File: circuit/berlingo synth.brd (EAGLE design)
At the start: 76.2 x 76.2 mm, 59 parts, among them IC4 LM358N, SW1 OS102011MA1Q

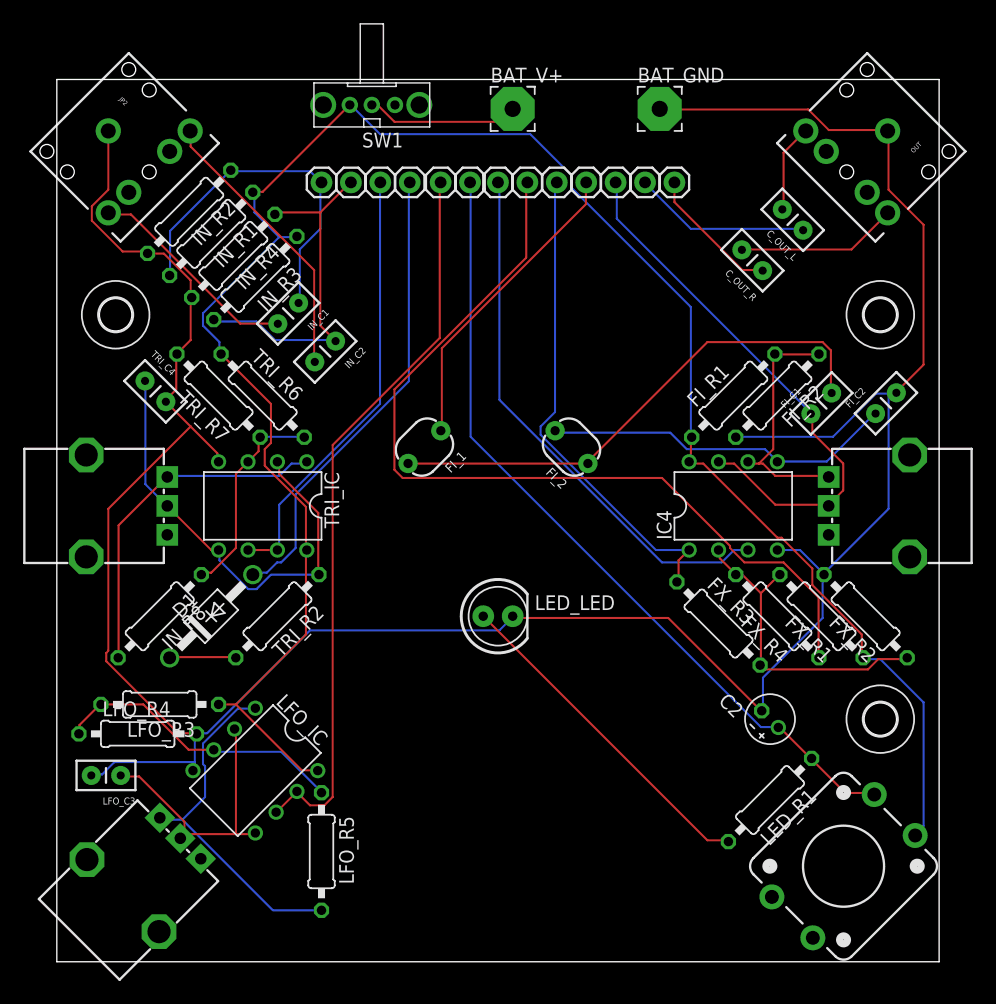
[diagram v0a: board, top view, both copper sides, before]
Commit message: Updated Parts and changed a few part names
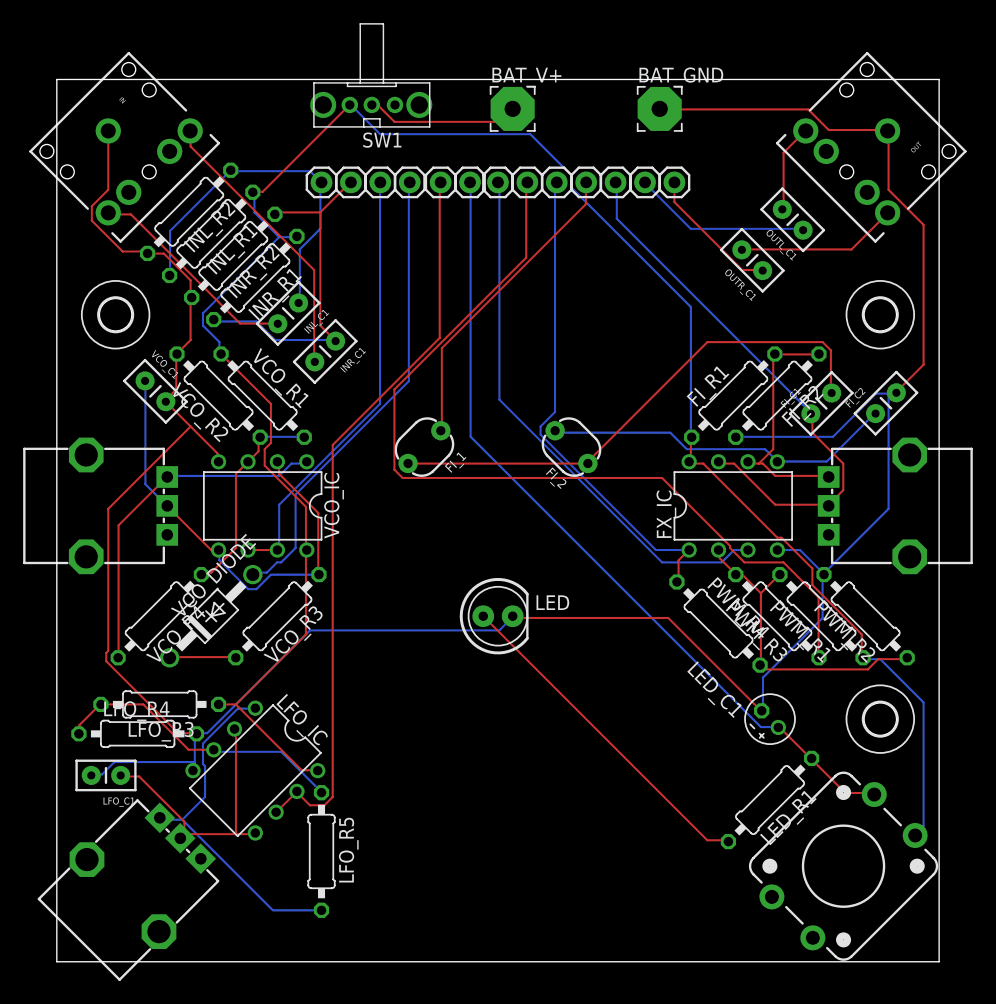
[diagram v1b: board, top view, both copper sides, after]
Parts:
- renumbered C2 to LED_C1, C_OUT_L to OUTL_C1, C_OUT_R to OUTR_C1, D1 to VCO_DIODE, FX_R1 to PWM_R1, FX_R2 to PWM_R2, FX_R3 to PWM_R4, FX_R4 to PWM_R3, IC4 to FX_IC, IN_C1 to INL_C1, IN_C2 to INR_C1, IN_L to INL, IN_R to INR, IN_R1 to INL_R1, IN_R2 to INL_R2, IN_R3 to INR_R1, IN_R4 to INR_R2, IN_R8 to VCO_R4, JP2 to IN, LED_LED to LED, LFO_C3 to LFO_C1, OUTA to OUTL, OUTB to OUTR, TRI_C4 to VCO_C1, TRI_IC to VCO_IC, TRI_PITCH to VCO_PITCH, TRI_R2 to VCO_R3, TRI_R6 to VCO_R1, TRI_R7 to VCO_R2, ~VCO to VCO~
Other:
- board text added: "Use eagle 6.6 to export!"
- board text removed: "tofstuff"

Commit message: Update BOM, increased trace sizes and added more silkscreen info
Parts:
- added H3: MOUNT-HOLE2.8, holes:2,8
- moved LFO_R3 0.57 mm to (8.38, 22.5), turned to 0 degrees
- moved LFO_R4 0.36 mm to (6.73, 19.9), turned to 180 degrees
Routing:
- net VIN: track 172.0 -> 244.1 mm
- net GND: track 238.7 -> 270.9 mm
- net N$14: track 30.7 -> 49.8 mm
- net FILTER_IN: track 26.7 -> 42.7 mm
- net N$21: track 30.5 -> 43.0 mm
- net N$6: track 29.3 -> 41.7 mm
- net N$8: track 44.9 -> 53.1 mm
- net N$22: track 24.1 -> 31.1 mm
- net N$7: track 30.5 -> 36.4 mm, vias 0 -> 1
- net PWM_OUT: track 42.6 -> 47.3 mm, vias 0 -> 1
- net N$9: track 11.8 -> 15.2 mm
- net LFO: track 63.4 -> 66.7 mm
- net N$5: track 76.1 -> 79.1 mm, vias 0 -> 1
- net N$12: track 15.4 -> 18.2 mm
- net N$24: track 13.9 -> 16.6 mm
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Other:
- board text added: "200K"
- board text added: "50K"
- board text added: "BERLINGO SYNTH 0.03"
- board text added: "ON"
- board text removed: "BERLINGO SYNTH 0.02"

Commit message: Euh...
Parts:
- added LED_C2: 100uF, rcl:E2,5-6
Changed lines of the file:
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@@
 <element name="INR" library="TOF" package="1X01_SIDE_NAME" value="IN(R)" x="25.4" y="67.31" rot="SR270"/>
 <element name="H3" library="holes" package="2,8" value="MOUNT-HOLE2.8" x="45.72" y="72.39"/>
+<element name="LED_C2" library="rcl" package="E2,5-6" value="100uF" x="45.720003125" y="20.846053125" rot="R45"/>
 </elements>
 <signals>
